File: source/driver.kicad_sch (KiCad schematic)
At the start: 58 parts, among them U10 TX4130L/PW2902, U2 AMS1117-3.3, U3 MC74VHC1G66, U4 EG3112, U5 MC74VHC1G66, U6 XL1509-5.0E1, U7 EG3112, U8 MC74VHC1G66, U9 EG3112

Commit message: First 4 layer order at JLCPCB
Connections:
- net GND: now also C14.2, C16.2
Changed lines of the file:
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@@
   (junction (at 143.51 175.26) (diameter 0) (color 0 0 0 0)
   )
+  (junction (at 101.6 68.58) (diameter 0) (color 0 0 0 0)
+  )
   (junction (at 68.58 58.42) (diameter 0) (color 0 0 0 0)
   )
   (junction (at 170.18 68.58) (diameter 0) (color 0 0 0 0)
   )
-  (junction (at 101.6 68.58) (diameter 0) (color 0 0 0 0)
-  )
   (junction (at 48.26 180.34) (diameter 0) (color 0 0 0 0)
   )
@@
   (junction (at 207.01 143.51) (diameter 0) (color 0 0 0 0)
   )
+  (junction (at 119.38 68.58) (diameter 0) (color 0 0 0 0)
+  )
   (junction (at 119.38 39.37) (diameter 0) (color 0 0 0 0)
   )
@@
     (stroke (width 0) (type default) (color 0 0 0 0))
   )
-  (wire (pts (xy 119.38 66.04) (xy 119.38 69.85))
+  (wire (pts (xy 119.38 66.04) (xy 119.38 68.58))
     (stroke (width 0) (type default) (color 0 0 0 0))
   )
@@
     (stroke (width 0) (type default) (color 0 0 0 0))
   )
+  (wire (pts (xy 119.38 68.58) (xy 119.38 69.85))
+    (stroke (width 0) (type default) (color 0 0 0 0))
+  )
   (wire (pts (xy 207.01 157.48) (xy 240.03 157.48))
     (stroke (width 0) (type default) (color 0 0 0 0))
@@
   (symbol (lib_id "power:+12V") (at 119.38 36.83 0) (mirror y) (unit 1)
     (in_bom yes) (on_board yes)
-    (property "Reference" "#PWR035" (id 0) (at 119.38 40.64 0)
+    (property "Reference" "#PWR033" (id 0) (at 119.38 40.64 0)
       (effects (font (size 1.27 1.27)) hide)
     )
@@
   (symbol (lib_id "power:VCC") (at 78.74 166.37 0) (unit 1)
     (in_bom yes) (on_board yes)
-    (property "Reference" "#PWR027" (id 0) (at 78.74 170.18 0)
+    (property "Reference" "#PWR025" (id 0) (at 78.74 170.18 0)
       (effects (font (size 1.27 1.27)) hide)
     )
@@
   (symbol (lib_id "power:+12V") (at 278.13 120.65 270) (mirror x) (unit 1)
     (in_bom yes) (on_board yes)
-    (property "Reference" "#PWR048" (id 0) (at 274.32 120.65 0)
+    (property "Reference" "#PWR046" (id 0) (at 274.32 120.65 0)
       (effects (font (size 1.27 1.27)) hide)
     )
@@
   (symbol (lib_id "power:+12V") (at 114.3 184.15 270) (unit 1)
     (in_bom yes) (on_board yes) (fields_autoplaced)
-    (property "Reference" "#PWR033" (id 0) (at 110.49 184.15 0)
+    (property "Reference" "#PWR031" (id 0) (at 110.49 184.15 0)
       (effects (font (size 1.27 1.27)) hide)
     )
@@
   (symbol (lib_id "power:GND") (at 276.86 138.43 0) (unit 1)
     (in_bom yes) (on_board yes)
-    (property "Reference" "#PWR047" (id 0) (at 276.86 144.78 0)
+    (property "Reference" "#PWR045" (id 0) (at 276.86 144.78 0)
       (effects (font (size 1.27 1.27)) hide)
     )
@@
   (symbol (lib_id "power:GND") (at 78.74 181.61 0) (unit 1)
     (in_bom yes) (on_board yes) (fields_autoplaced)
-    (property "Reference" "#PWR028" (id 0) (at 78.74 187.96 0)
+    (property "Reference" "#PWR026" (id 0) (at 78.74 187.96 0)
       (effects (font (size 1.27 1.27)) hide)
     )
@@
   (symbol (lib_id "power:GND") (at 40.64 128.27 0) (unit 1)
     (in_bom yes) (on_board yes)
-    (property "Reference" "#PWR023" (id 0) (at 40.64 134.62 0)
+    (property "Reference" "#PWR021" (id 0) (at 40.64 134.62 0)
       (effects (font (size 1.27 1.27)) hide)
     )
@@
   (symbol (lib_id "power:GND") (at 266.7 35.56 0) (unit 1)
     (in_bom yes) (on_board yes)
-    (property "Reference" "#PWR046" (id 0) (at 266.7 41.91 0)
+    (property "Reference" "#PWR044" (id 0) (at 266.7 41.91 0)
       (effects (font (size 1.27 1.27)) hide)
     )
@@
   (symbol (lib_id "power:GND") (at 83.82 129.54 0) (unit 1)
     (in_bom yes) (on_board yes)
-    (property "Reference" "#PWR030" (id 0) (at 83.82 135.89 0)
+    (property "Reference" "#PWR028" (id 0) (at 83.82 135.89 0)
       (effects (font (size 1.27 1.27)) hide)
     )
@@
   (symbol (lib_id "power:GND") (at 113.03 102.87 0) (unit 1)
     (in_bom yes) (on_board yes)
-    (property "Reference" "#PWR032" (id 0) (at 113.03 109.22 0)
+    (property "Reference" "#PWR030" (id 0) (at 113.03 109.22 0)
       (effects (font (size 1.27 1.27)) hide)
     )
@@
   (symbol (lib_id "power:VCC") (at 83.82 104.14 0) (unit 1)
     (in_bom yes) (on_board yes)
-    (property "Reference" "#PWR029" (id 0) (at 83.82 107.95 0)
+    (property "Reference" "#PWR027" (id 0) (at 83.82 107.95 0)
       (effects (font (size 1.27 1.27)) hide)
     )
@@
   (symbol (lib_id "power:GND") (at 95.25 190.5 0) (mirror y) (unit 1)
     (in_bom yes) (on_board yes) (fields_autoplaced)
-    (property "Reference" "#PWR031" (id 0) (at 95.25 196.85 0)
+    (property "Reference" "#PWR029" (id 0) (at 95.25 196.85 0)
       (effects (font (size 1.27 1.27)) hide)
     )
@@
   (symbol (lib_id "power:+12V") (at 187.96 34.29 0) (mirror y) (unit 1)
     (in_bom yes) (on_board yes)
-    (property "Reference" "#PWR042" (id 0) (at 187.96 38.1 0)
+    (property "Reference" "#PWR040" (id 0) (at 187.96 38.1 0)
       (effects (font (size 1.27 1.27)) hide)
     )
@@
   (symbol (lib_id "power:GND") (at 52.07 69.85 0) (unit 1)
     (in_bom yes) (on_board yes)
-    (property "Reference" "#PWR025" (id 0) (at 52.07 76.2 0)
+    (property "Reference" "#PWR023" (id 0) (at 52.07 76.2 0)
       (effects (font (size 1.27 1.27)) hide)
     )
@@
   (symbol (lib_id "power:+12V") (at 52.07 36.83 0) (mirror y) (unit 1)
     (in_bom yes) (on_board yes)
-    (property "Reference" "#PWR024" (id 0) (at 52.07 40.64 0)
+    (property "Reference" "#PWR022" (id 0) (at 52.07 40.64 0)
       (effects (font (size 1.27 1.27)) hide)
     )
@@
   (symbol (lib_id "power:VCC") (at 40.64 102.87 0) (unit 1)
     (in_bom yes) (on_board yes)
-    (property "Reference" "#PWR022" (id 0) (at 40.64 106.68 0)
+    (property "Reference" "#PWR020" (id 0) (at 40.64 106.68 0)
       (effects (font (size 1.27 1.27)) hide)
     )
@@
   (symbol (lib_id "power:GND") (at 156.21 102.87 0) (unit 1)
     (in_bom yes) (on_board yes)
-    (property "Reference" "#PWR039" (id 0) (at 156.21 109.22 0)
+    (property "Reference" "#PWR037" (id 0) (at 156.21 109.22 0)
       (effects (font (size 1.27 1.27)) hide)
     )
@@
   (symbol (lib_id "power:VCC") (at 127 104.14 0) (unit 1)
     (in_bom yes) (on_board yes)
-    (property "Reference" "#PWR037" (id 0) (at 127 107.95 0)
+    (property "Reference" "#PWR035" (id 0) (at 127 107.95 0)
       (effects (font (size 1.27 1.27)) hide)
     )
@@
   (symbol (lib_id "power:GND") (at 119.38 69.85 0) (unit 1)
     (in_bom yes) (on_board yes)
-    (property "Reference" "#PWR036" (id 0) (at 119.38 76.2 0)
+    (property "Reference" "#PWR034" (id 0) (at 119.38 76.2 0)
       (effects (font (size 1.27 1.27)) hide)
     )
@@
   (symbol (lib_id "power:+5V") (at 160.02 173.99 0) (unit 1)
     (in_bom yes) (on_board yes) (fields_autoplaced)
-    (property "Reference" "#PWR040" (id 0) (at 160.02 177.8 0)
+    (property "Reference" "#PWR038" (id 0) (at 160.02 177.8 0)
       (effects (font (size 1.27 1.27)) hide)
     )
@@
   (symbol (lib_id "power:GND") (at 69.85 101.6 0) (unit 1)
     (in_bom yes) (on_board yes)
-    (property "Reference" "#PWR026" (id 0) (at 69.85 107.95 0)
+    (property "Reference" "#PWR024" (id 0) (at 69.85 107.95 0)
       (effects (font (size 1.27 1.27)) hide)
     )
@@
   (symbol (lib_id "power:GND") (at 127 129.54 0) (unit 1)
     (in_bom yes) (on_board yes)
-    (property "Reference" "#PWR038" (id 0) (at 127 135.89 0)
+    (property "Reference" "#PWR036" (id 0) (at 127 135.89 0)
       (effects (font (size 1.27 1.27)) hide)
     )
@@
   (symbol (lib_id "power:GND") (at 187.96 69.85 0) (unit 1)
     (in_bom yes) (on_board yes)
-    (property "Reference" "#PWR043" (id 0) (at 187.96 76.2 0)
+    (property "Reference" "#PWR041" (id 0) (at 187.96 76.2 0)
       (effects (font (size 1.27 1.27)) hide)
     )
@@
   (symbol (lib_id "power:GND") (at 207.01 120.65 270) (unit 1)
     (in_bom yes) (on_board yes)
-    (property "Reference" "#PWR044" (id 0) (at 200.66 120.65 0)
+    (property "Reference" "#PWR042" (id 0) (at 200.66 120.65 0)
       (effects (font (size 1.27 1.27)) hide)
     )
@@
   (symbol (lib_id "power:+5V") (at 26.67 166.37 0) (unit 1)
     (in_bom yes) (on_board yes) (fields_autoplaced)
-    (property "Reference" "#PWR021" (id 0) (at 26.67 170.18 0)
+    (property "Reference" "#PWR019" (id 0) (at 26.67 170.18 0)
       (effects (font (size 1.27 1.27)) hide)
     )
@@
   (symbol (lib_id "power:+12V") (at 212.09 153.67 0) (mirror x) (unit 1)
     (in_bom yes) (on_board yes)
-    (property "Reference" "#PWR045" (id 0) (at 212.09 149.86 0)
+    (property "Reference" "#PWR043" (id 0) (at 212.09 149.86 0)
       (effects (font (size 1.27 1.27)) hide)
     )
@@
   (symbol (lib_id "power:+12V") (at 116.84 171.45 0) (unit 1)
     (in_bom yes) (on_board yes) (fields_autoplaced)
-    (property "Reference" "#PWR034" (id 0) (at 116.84 175.26 0)
+    (property "Reference" "#PWR032" (id 0) (at 116.84 175.26 0)
       (effects (font (size 1.27 1.27)) hide)
     )
@@
   (symbol (lib_id "power:GND") (at 171.45 165.1 0) (unit 1)
     (in_bom yes) (on_board yes)
-    (property "Reference" "#PWR041" (id 0) (at 171.45 171.45 0)
+    (property "Reference" "#PWR039" (id 0) (at 171.45 171.45 0)
       (effects (font (size 1.27 1.27)) hide)
     )

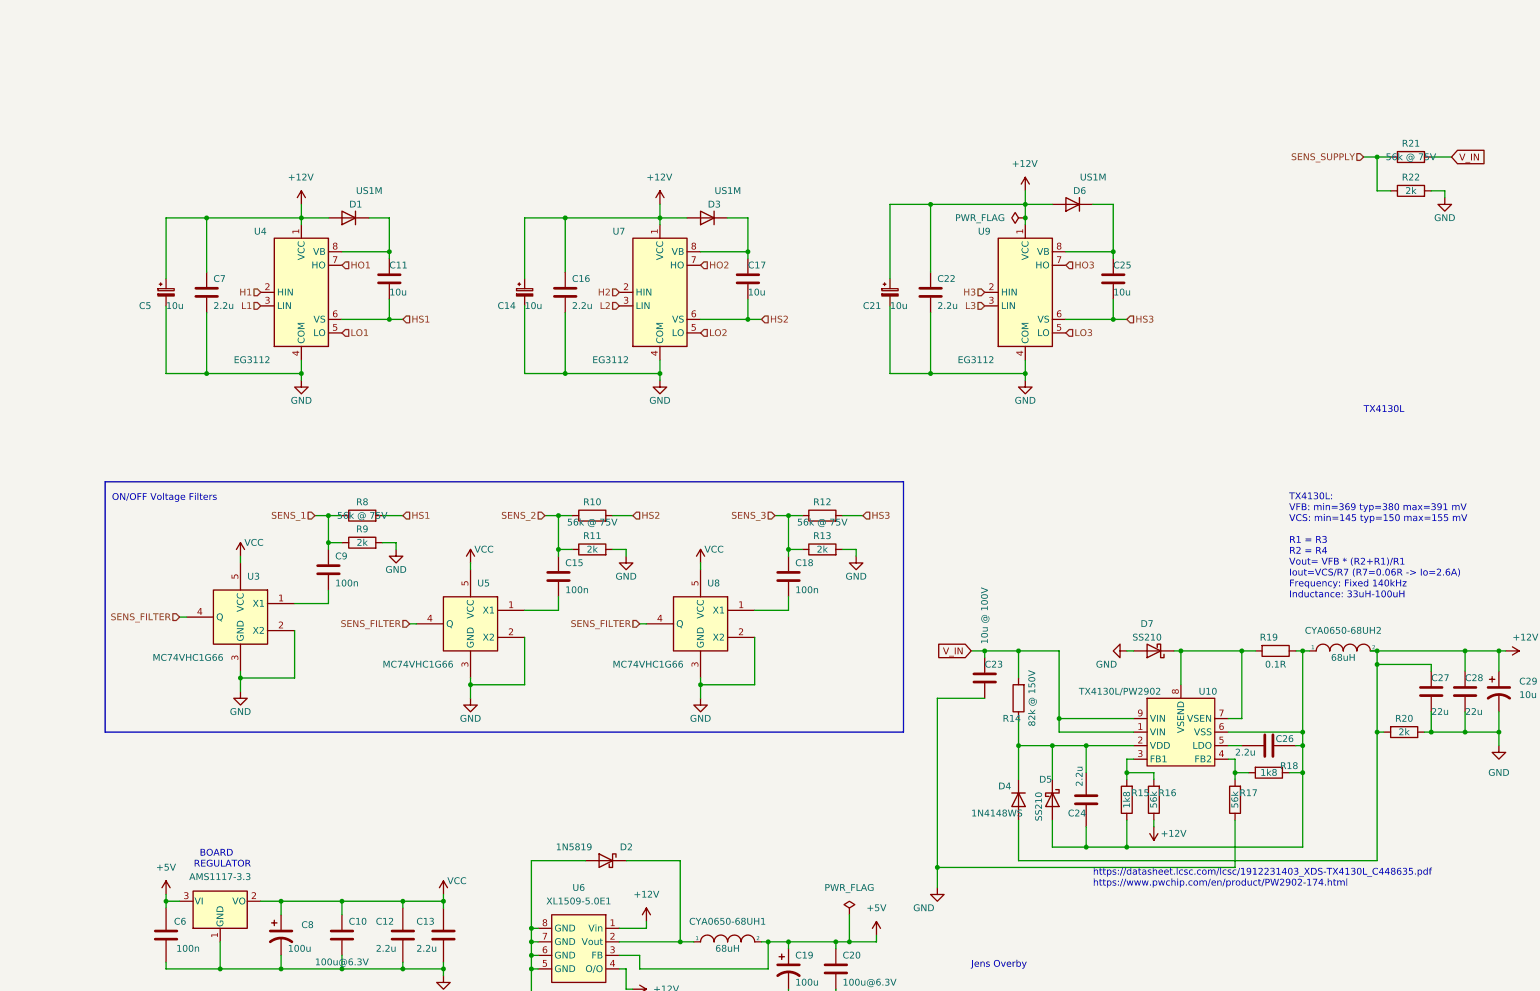
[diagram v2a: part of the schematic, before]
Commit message: Add files via upload
Filter resistor on current op-amps changed from 30k to 150R
Mosfets at 45 deg angle
Changed layout of power supply
Cut through center of board
Unnecessary components near mosfets removed
Voltage filters removed again
Crystal suspected noise source - moved to back of board
Current sensing moved to in0 - in2 (PA0-PA2)
Voltage sensing moved to in11-in13
Supply voltage moved to in10
Mosfets can now be attached to heat-sink plate using screws (that can be tightened throug holes in the board)
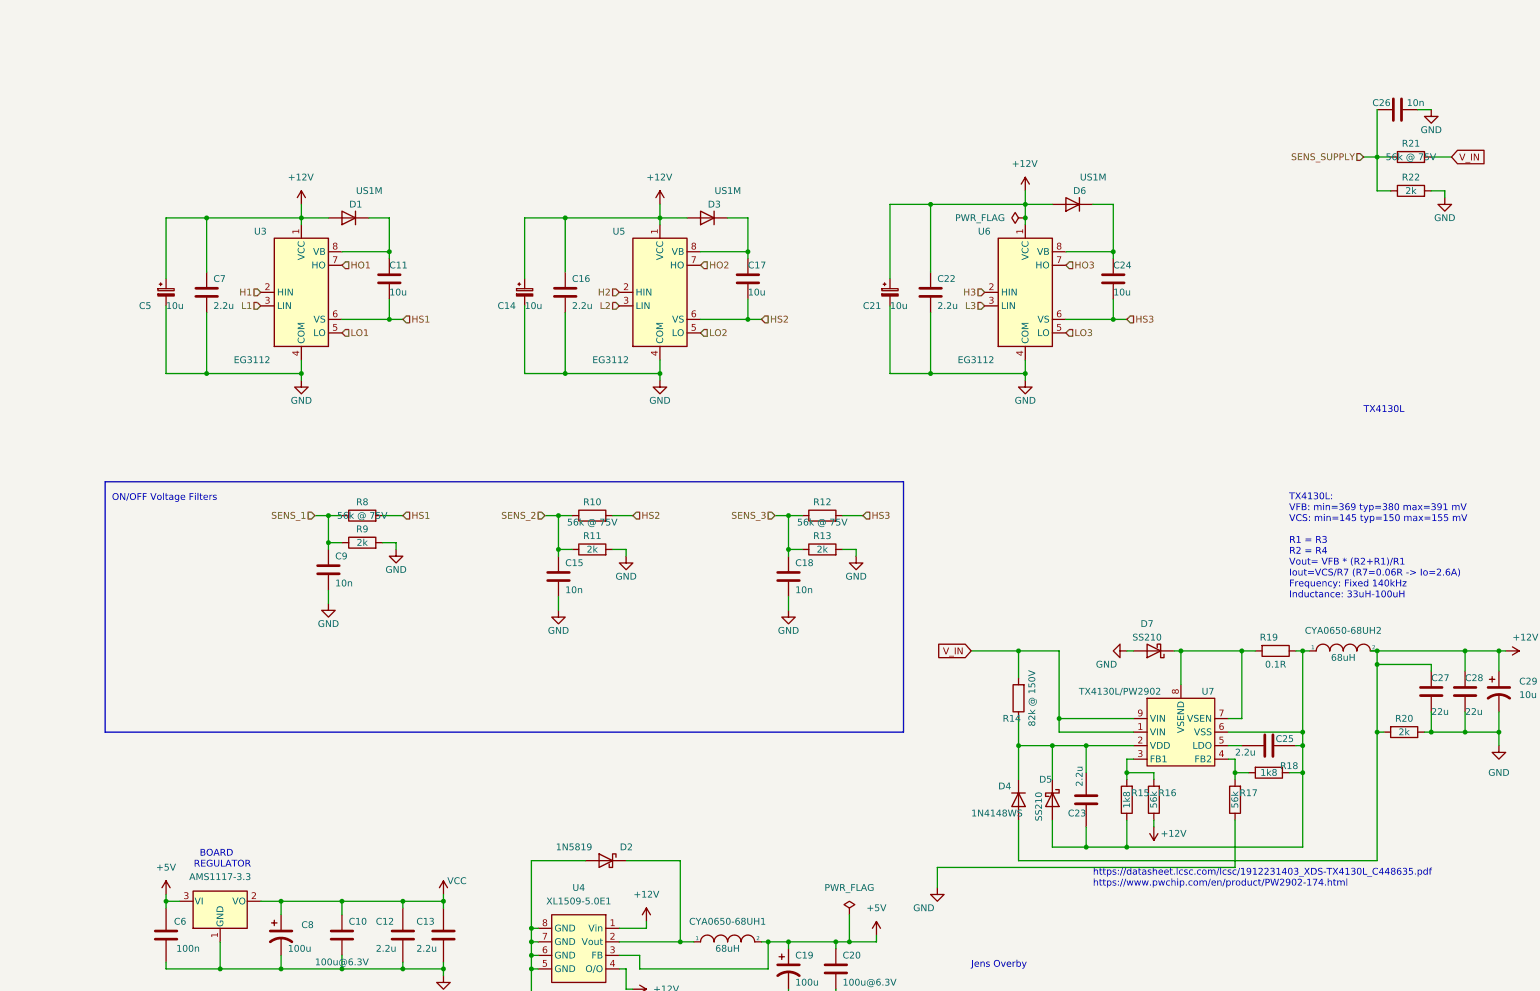
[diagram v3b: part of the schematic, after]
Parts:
- removed C23: 10u @ 100V, Capacitor_SMD:C_2220_5650Metric, symbol Device:C
- removed U3, U5, U8: MC74VHC1G66, Package_TO_SOT_SMD:SOT-353_SC-70-5, symbol 74xGxx:74AHC1G4210
- added C26: 10n, Capacitor_SMD:C_0603_1608Metric, symbol Device:C
- C15, C18, C9: value 100n -> 10n; LCSC C14663 -> C57112
- renumbered C24 to C23, C25 to C24, C26 to C25, U4 to U3, U6 to U4, U7 to U5, U9 to U6, U10 to U7
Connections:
- net GND: now also C15.2, C18.2, C9.2, C26.2
- net SENS_SUPPLY: now also C26.1
